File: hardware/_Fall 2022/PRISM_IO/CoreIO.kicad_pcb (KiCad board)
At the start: 2 copper layers, 61 x 88.9 mm, 29 parts, among them J1 CORE_FC, J2 COTS_SWITCH_PLUG, J3 PYRO 1, J4 PYRO 2, Q1 AO3400A, Q2 AO3400A

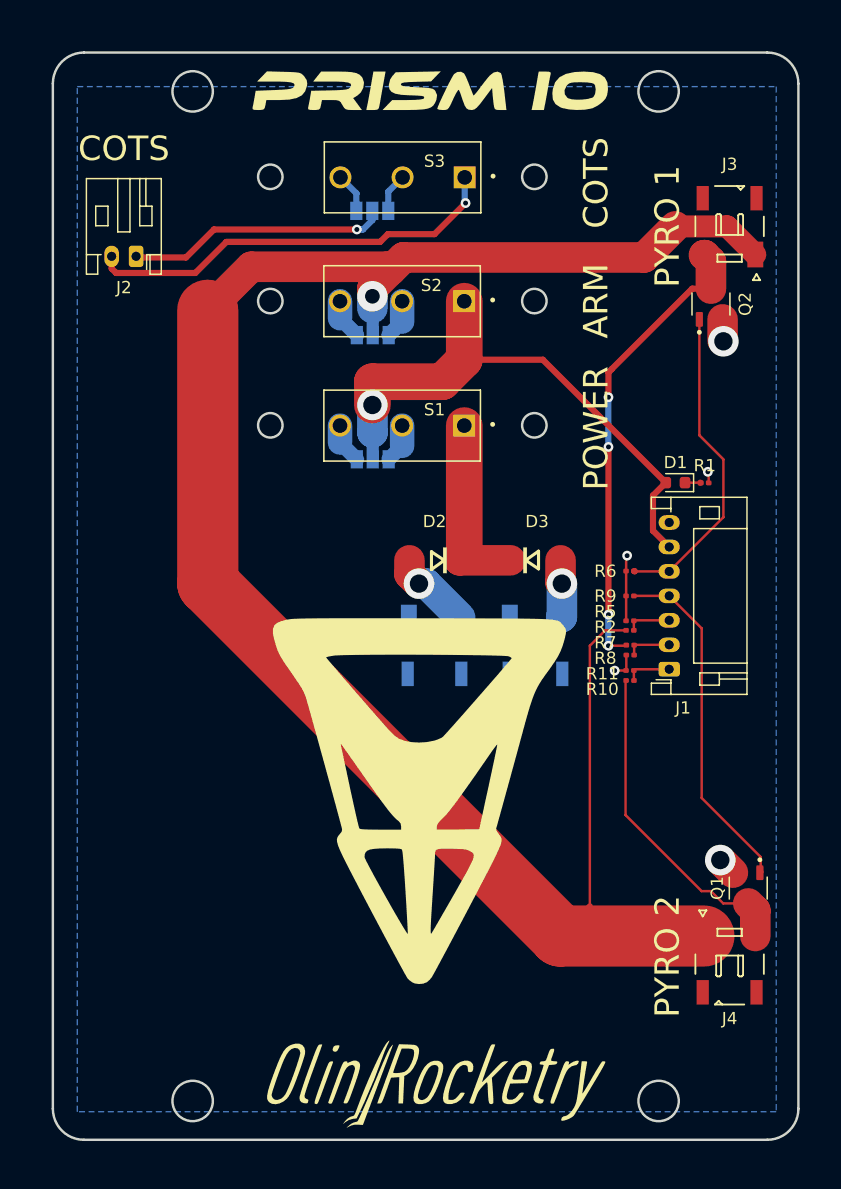
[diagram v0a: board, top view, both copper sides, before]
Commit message: add mounting holes and update resistor size
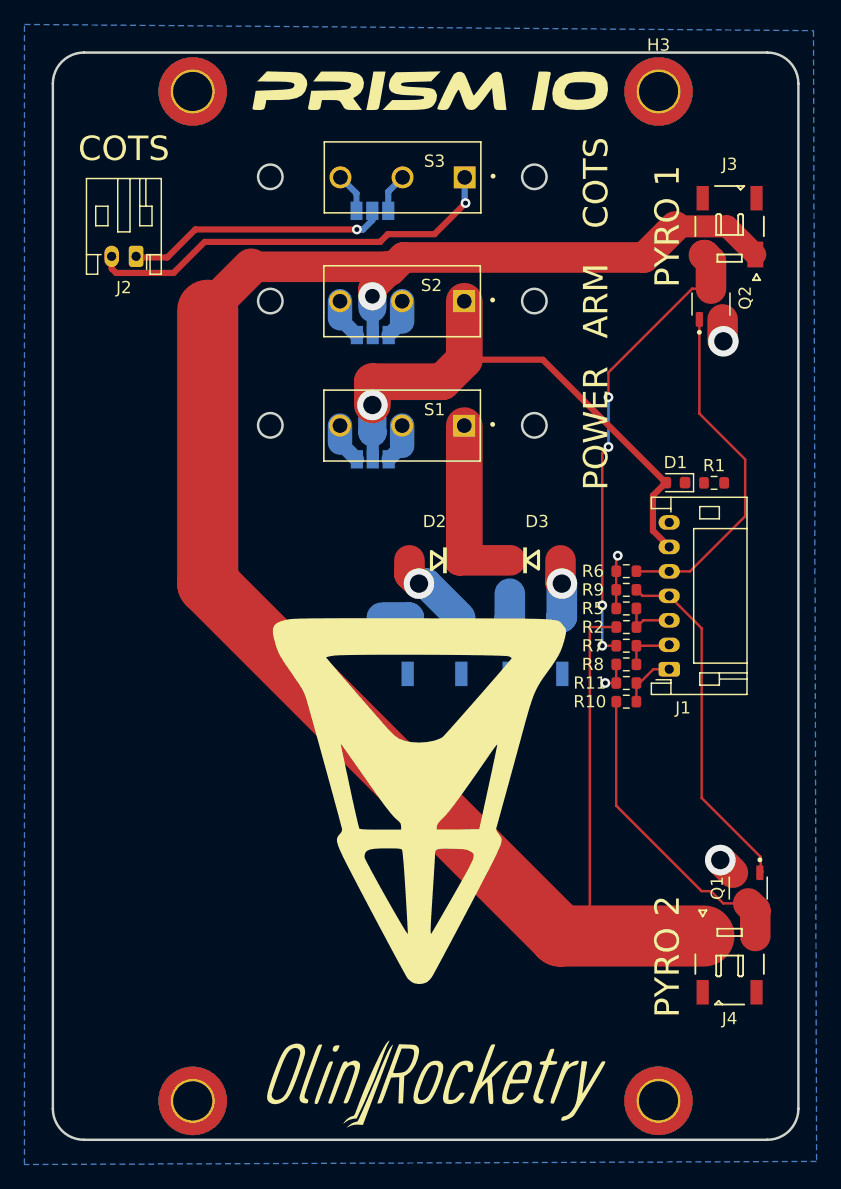
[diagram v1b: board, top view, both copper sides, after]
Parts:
- added H1: MountingHole_Pad, MountingHole:MountingHole_3.2mm_M3_DIN965_Pad_TopBottom, F.Cu at (128.8, 53.7)
- added H2: MountingHole, MountingHole:MountingHole_3.2mm_M3_DIN965_Pad_TopBottom, F.Cu at (166.9, 136.3)
- added H3: MountingHole, MountingHole:MountingHole_3.2mm_M3_DIN965_Pad_TopBottom, F.Cu at (166.9, 53.7)
- added H4: MountingHole, MountingHole:MountingHole_3.2mm_M3_DIN965_Pad_TopBottom, F.Cu at (128.8, 136.3)
- R1, R10, R11, R2, R5, R6, R7, R8, R9: footprint Resistor_SMD:R_0201_0603Metric -> Resistor_SMD:R_0603_1608Metric
- moved R10 1.76 mm to (164.3, 103.6)
- moved R11 1.07 mm to (164.3, 102.1)
- moved R5 1.05 mm to (164.3, 96.0)
- moved R8 0.83 mm to (164.3, 100.6)
- moved R1 0.76 mm to (171.4, 85.7)
- moved R9 0.58 mm to (164.3, 94.5)
- moved R2 0.39 mm to (164.3, 97.5)
- moved R7 0.32 mm to (164.3, 99.1)
- moved R6 0.30 mm to (164.3, 93.0)
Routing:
- net GND: track 12.1 -> 17.3 mm, vias 5 -> 4
- net /PYRO 1: track 26.1 -> 28.4 mm
- net Net-(J4-Pad2): track 26.9 -> 25.5 mm
- net Net-(D1-Pad1): track 1.26 -> 0.00 mm
- net /CONT 2: track 3.73 -> 4.67 mm
- net /ARM: track 3.69 -> 4.43 mm
- net /CONT 1: track 3.65 -> 4.28 mm
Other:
- outline, holes or cut-outs redrawn

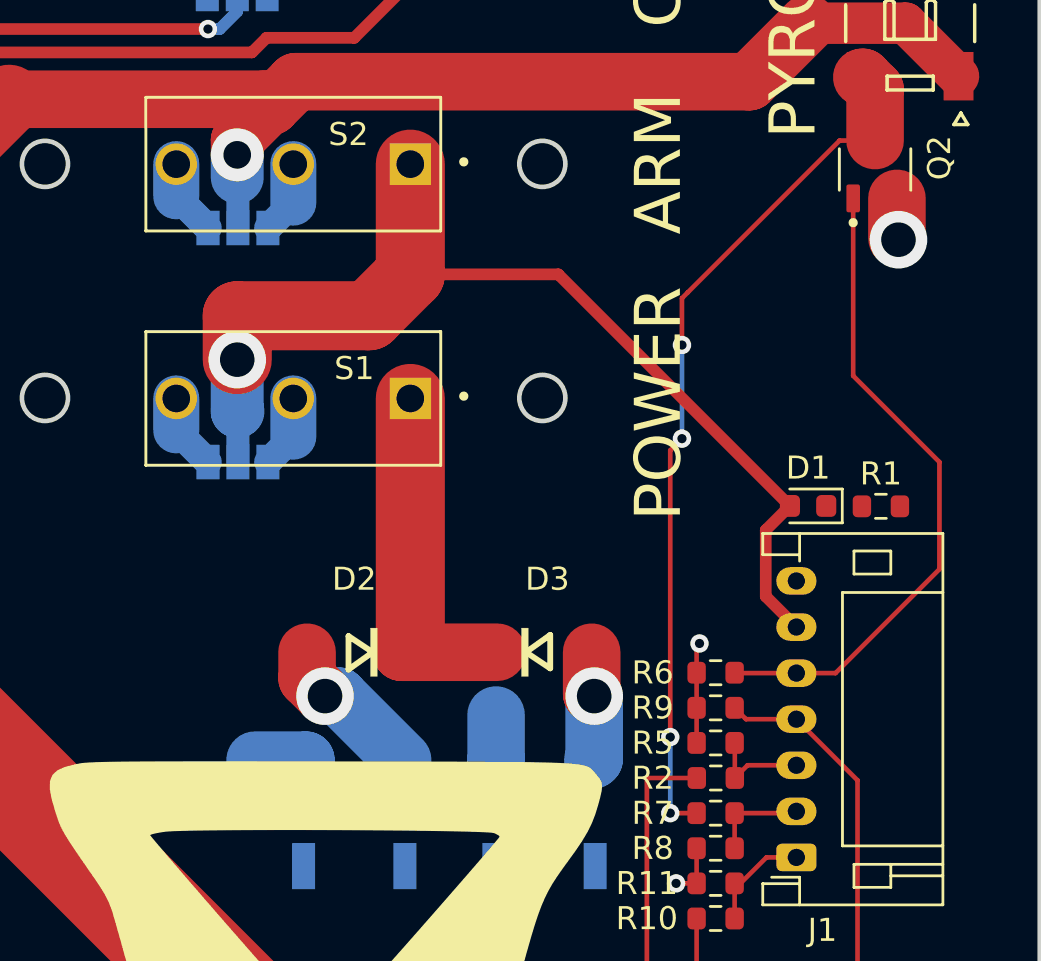
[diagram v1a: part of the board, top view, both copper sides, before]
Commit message: Completed IO layout, added board 1 plated holes
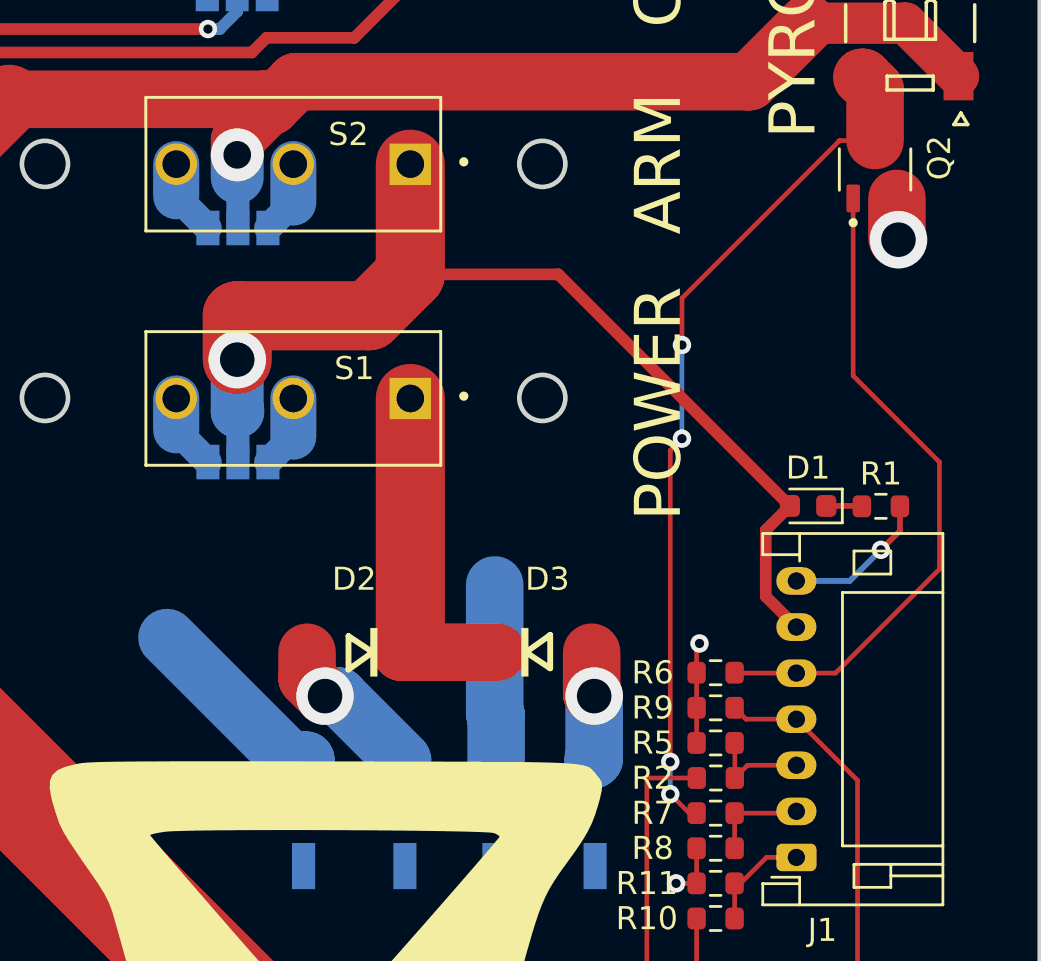
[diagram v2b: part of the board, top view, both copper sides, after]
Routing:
- net GND: track 17.3 -> 33.4 mm, vias 4 -> 5
- net Net-(D1-Pad1): track 0.00 -> 1.56 mm
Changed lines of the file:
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@@
   (segment (start 163.45 96.012) (end 163.45 94.488) (width 0.2032) (layer "F.Cu") (net 7))
   (segment (start 172.989 117.617) (end 171.958 116.586) (width 2.5) (layer "F.Cu") (net 7))
+  (segment (start 172.275 86.805) (end 171.45 87.63) (width 0.25) (layer "F.Cu") (net 7))
   (segment (start 172.146 72.375) (end 172.146 74.102) (width 2.5) (layer "F.Cu") (net 7))
   (segment (start 163.45 102.108) (end 162.56 102.108) (width 0.2032) (layer "F.Cu") (net 7))
+  (segment (start 172.275 85.741317) (end 172.275 86.805) (width 0.25) (layer "F.Cu") (net 7))
   (segment (start 163.45 102.108) (end 163.45 100.584) (width 0.2032) (layer "F.Cu") (net 7))
   (segment (start 163.45 91.82) (end 163.576 91.694) (width 0.2032) (layer "F.Cu") (net 7))
   (segment (start 163.45 92.964) (end 163.45 91.82) (width 0.2032) (layer "F.Cu") (net 7))
   (via (at 171.958 116.586) (size 2.5) (drill 1.5) (layers "F.Cu" "B.Cu") (net 7))
+  (via (at 171.45 87.63) (size 0.8) (drill 0.4) (layers "F.Cu" "B.Cu") (net 7))
   (via (at 172.212 74.168) (size 2.5) (drill 1.5) (layers "F.Cu" "B.Cu") (net 7))
   (via (at 162.56 102.108) (size 0.8) (drill 0.4) (layers "F.Cu" "B.Cu") (net 7))
   (via (at 163.576 91.694) (size 0.8) (drill 0.4) (layers "F.Cu" "B.Cu") (net 7))
+  (segment (start 145.782 96.76) (end 140.462 91.44) (width 2.5) (layer "B.Cu") (net 7))
+  (segment (start 154.745 94.801) (end 154.686 94.742) (width 2.5) (layer "B.Cu") (net 7))
+  (segment (start 154.686 94.742) (end 154.686 89.154) (width 2.5) (layer "B.Cu") (net 7))
   (segment (start 146.49 96.76) (end 146.49 97.468) (width 2.5) (layer "B.Cu") (net 7))
-  (segment (start 146.49 97.468) (end 147.066 98.044) (width 2.5) (layer "B.Cu") (net 7))
   (segment (start 154.745 96.76) (end 154.745 94.801) (width 2.5) (layer "B.Cu") (net 7))
-  (segment (start 154.745 96.76) (end 154.745 97.985) (width 2.5) (layer "B.Cu") (net 7))
-  (segment (start 146.49 96.76) (end 144.286 96.76) (width 2.5) (layer "B.Cu") (net 7))
-  (segment (start 162.306 83.312) (end 162.306 95.758) (width 0.2032) (layer "F.Cu") (net 8))
-  (segment (start 162.814 82.804) (end 162.306 83.312) (width 0.2032) (layer "F.Cu") (net 8))
+  (segment (start 146.49 96.76) (end 145.782 96.76) (width 2.5) (layer "B.Cu") (net 7))
+  (segment (start 170.098683 88.981317) (end 171.45 87.63) (width 0.25) (layer "B.Cu") (net 7))
+  (segment (start 167.780605 88.981317) (end 170.098683 88.981317) (width 0.25) (layer "B.Cu") (net 7))
+  (segment (start 162.814 78.74) (end 162.814 76.708) (width 0.2032) (layer "F.Cu") (net 8))
+  (segment (start 162.814 76.708) (end 169.657 69.865) (width 0.2032) (layer "F.Cu") (net 8))
+  (segment (start 162.306 98.234998) (end 163.131002 99.06) (width 0.2032) (layer "F.Cu") (net 8))
+  (segment (start 169.657 69.865) (end 171.196 69.865) (width 0.2032) (layer "F.Cu") (net 8))
   (segment (start 171.196 69.865) (end 171.196 67.646) (width 2.5) (layer "F.Cu") (net 8))
-  (segment (start 162.306 99.06) (end 163.45 99.06) (width 0.2032) (layer "F.Cu") (net 8))
-  (segment (start 162.814 76.708) (end 162.814 78.74) (width 0.2032) (layer "F.Cu") (net 8))
-  (segment (start 169.657 69.865) (end 163.068 76.454) (width 0.2032) (layer "F.Cu") (net 8))
-  (segment (start 171.196 69.865) (end 169.657 69.865) (width 0.2032) (layer "F.Cu") (net 8))
-  (segment (start 163.068 76.454) (end 162.814 76.708) (width 0.2032) (layer "F.Cu") (net 8))
+  (segment (start 162.306 96.832798) (end 162.306 83.312) (width 0.2032) (layer "F.Cu") (net 8))
+  (segment (start 163.131002 99.06) (end 163.45 99.06) (width 0.2032) (layer "F.Cu") (net 8))
+  (segment (start 162.306 83.312) (end 162.814 82.804) (width 0.2032) (layer "F.Cu") (net 8))
   (segment (start 170.67 67.12) (end 170.62 67.12) (width 2.5) (layer "F.Cu") (net 8))
   (segment (start 171.196 67.646) (end 170.67 67.12) (width 2.5) (layer "F.Cu") (net 8))
   (via (at 162.814 78.74) (size 0.8) (drill 0.4) (layers "F.Cu" "B.Cu") (net 8))
-  (via (at 162.306 95.758) (size 0.8) (drill 0.4) (layers "F.Cu" "B.Cu") (net 8))
-  (via (at 162.306 99.06) (size 0.8) (drill 0.4) (layers "F.Cu" "B.Cu") (net 8))
+  (via (at 162.306 96.832798) (size 0.8) (drill 0.4) (layers "F.Cu" "B.Cu") (net 8))
+  (via (at 162.306 98.234998) (size 0.8) (drill 0.4) (layers "F.Cu" "B.Cu") (net 8))
   (via (at 162.814 82.804) (size 0.8) (drill 0.4) (layers "F.Cu" "B.Cu") (net 8))
-  (segment (start 162.306 95.758) (end 162.306 99.06) (width 0.2032) (layer "B.Cu") (net 8))
   (segment (start 162.814 78.74) (end 162.814 82.804) (width 0.2032) (layer "B.Cu") (net 8))
+  (segment (start 162.306 96.832798) (end 162.306 98.234998) (width 0.2032) (layer "B.Cu") (net 8))
   (segment (start 150.64 92.075) (end 154.795 92.075) (width 2.5) (layer "F.Cu") (net 9))
   (segment (start 151.023176 81.059176) (end 151.023176 91.691824) (width 3) (layer "F.Cu") (net 9))
@@
   (segment (start 159.004 93.98) (end 159.004 96.701) (width 2.5) (layer "B.Cu") (net 13))
   (segment (start 159.004 96.701) (end 158.945 96.76) (width 2.5) (layer "B.Cu") (net 13))
+  (segment (start 169.076105 85.725) (end 170.608683 85.725) (width 0.25) (layer "F.Cu") (net 14))
+  (segment (start 170.608683 85.725) (end 170.625 85.741317) (width 0.25) (layer "F.Cu") (net 14))
   (segment (start 172.52 64.77) (end 168.275 64.77) (width 1.8) (layer "F.Cu") (net 15))
   (segment (start 144.674 68.072) (end 144.981 68.379) (width 2.5) (layer "F.Cu") (net 15))

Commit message: minor fixes
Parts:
- moved ? 0.59 mm to (147.6, 54.1)
- moved ? 0.25 mm to (148.3, 134.6)
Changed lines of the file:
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@@
   )
   (footprint "LOGO" (layer "F.Cu")
-    (at 148.59 134.62)
+    (at 148.336 134.62)
     (attr board_only exclude_from_pos_files exclude_from_bom)
     (fp_text reference "" (at 0 0) (layer "F.SilkS")
@@
   )
   (footprint "LOGO" (layer "F.Cu")
-    (at 148.113781 53.858316)
+    (at 147.574 54.102)
     (attr board_only exclude_from_pos_files exclude_from_bom)
     (fp_text reference "" (at 0 0) (layer "F.SilkS")
